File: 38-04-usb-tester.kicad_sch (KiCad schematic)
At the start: 64 parts, among them J1 Conn_1x05, J2 USB_C_12401832E402A, J3 USB_C_12401832E402A, J4 USB_Micro-B_KH-MICRO5P-JN, J5 USB_Mini-B_U-M-M5DD-W-1, J6 USB3_A_HC-USB3.0-L168-WP, SW1 SW_SPDT, SW2 ZX-1.27BM-4PSMD, U1 STM32C031K6Tx

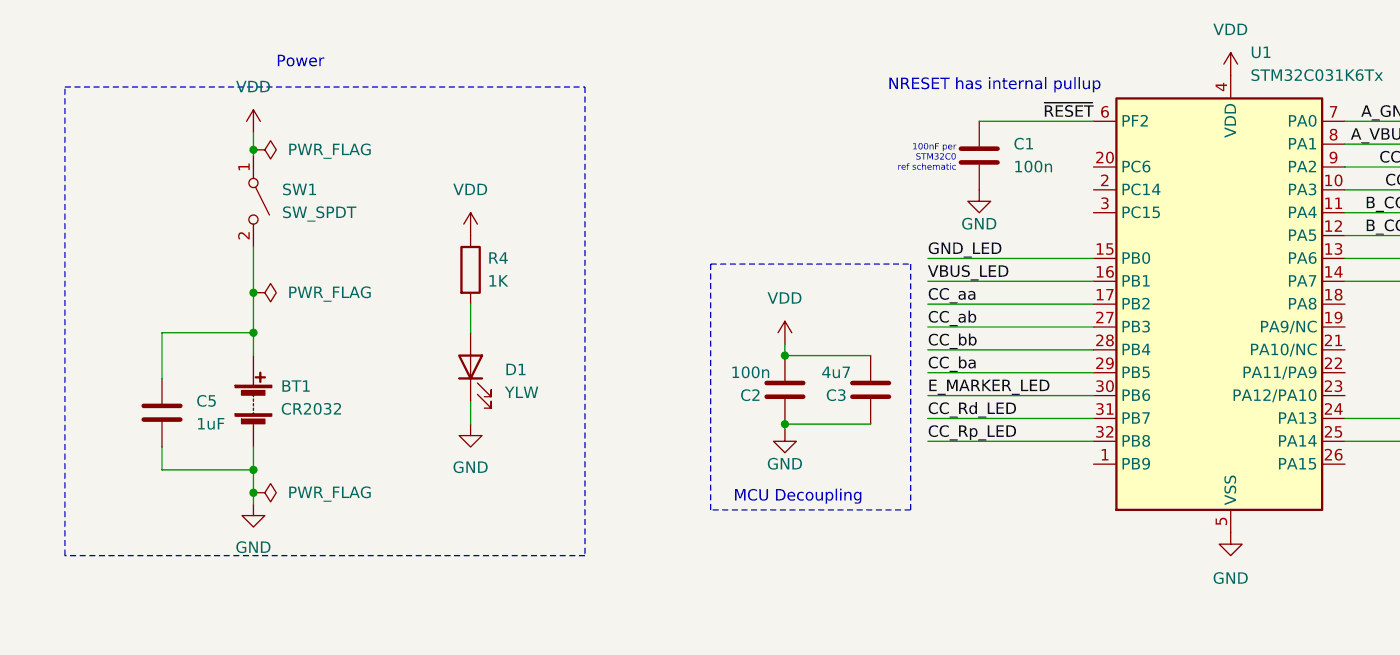
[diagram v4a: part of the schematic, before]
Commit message: more layout DRC fixes
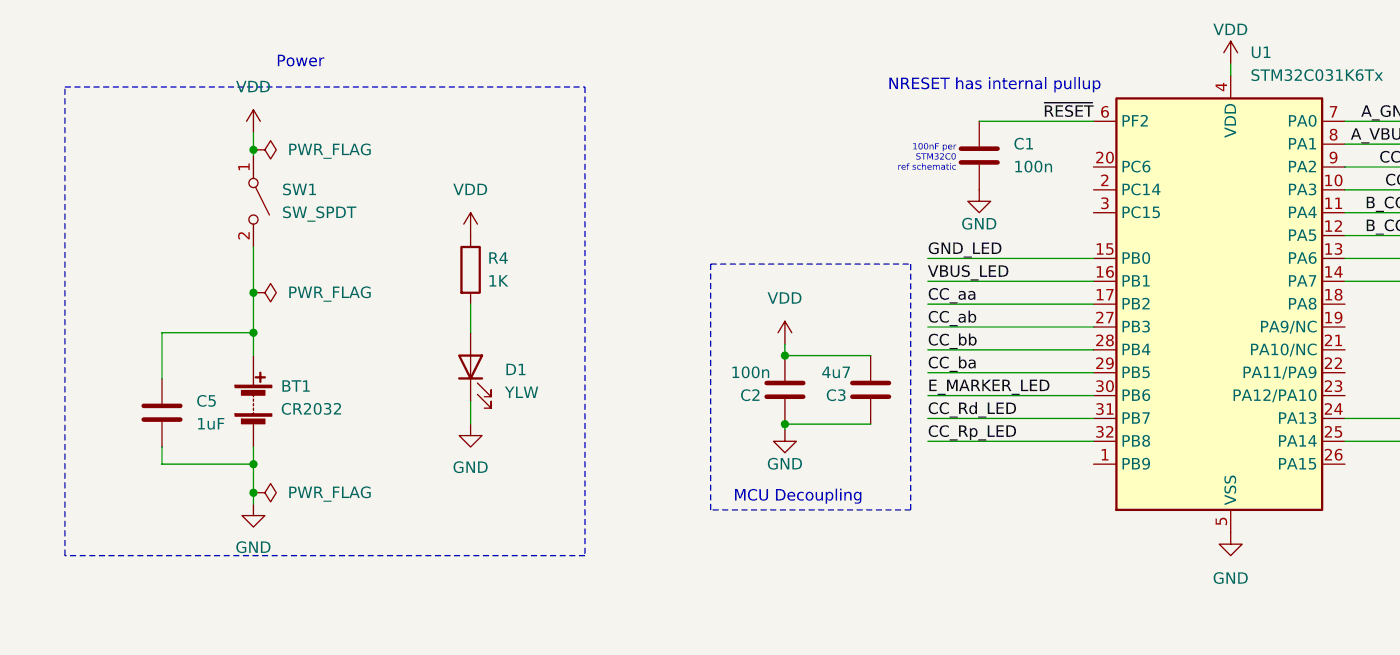
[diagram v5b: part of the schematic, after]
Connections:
- net VDD is gone; now on net VCC: U1.4 (VDD)
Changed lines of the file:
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@@
   (junction (at 218.44 139.7) (diameter 0) (color 0 0 0 0)
   )
-  (junction (at 50.165 71.12) (diameter 0) (color 0 0 0 0)
-  )
   (junction (at 182.245 106.68) (diameter 0) (color 0 0 0 0)
   )
@@
   (junction (at 45.085 163.195) (diameter 0) (color 0 0 0 0)
   )
+  (junction (at 50.165 70.485) (diameter 0) (color 0 0 0 0)
+  )
   (junction (at 367.03 161.925) (diameter 0) (color 0 0 0 0)
   )
@@
     (stroke (width 0) (type default))
   )
-  (wire (pts (xy 40.005 68.58) (xy 40.005 71.12))
-    (stroke (width 0) (type default))
-  )
   (wire (pts (xy 113.03 137.16) (xy 113.03 139.7))
     (stroke (width 0) (type default))
@@
     (stroke (width 0) (type default))
   )
-  (wire (pts (xy 40.005 71.12) (xy 50.165 71.12))
+  (wire (pts (xy 40.005 70.485) (xy 50.165 70.485))
     (stroke (width 0) (type default))
   )
@@
     (stroke (width 0) (type default))
   )
+  (wire (pts (xy 50.165 70.485) (xy 50.165 73.66))
+    (stroke (width 0) (type default))
+  )
   (wire (pts (xy 171.45 42.545) (xy 204.47 42.545))
     (stroke (width 0) (type default))
@@
     (stroke (width 0) (type default))
   )
-  (wire (pts (xy 50.165 68.58) (xy 50.165 71.12))
-    (stroke (width 0) (type default))
-  )
   (wire (pts (xy 183.515 154.94) (xy 203.835 154.94))
     (stroke (width 0) (type default))
@@
     (stroke (width 0) (type default))
   )
+  (wire (pts (xy 40.005 70.485) (xy 40.005 68.58))
+    (stroke (width 0) (type default))
+  )
   (wire (pts (xy 109.22 58.42) (xy 118.745 58.42))
     (stroke (width 0) (type default))
@@
     (stroke (width 0) (type default))
   )
+  (wire (pts (xy 158.75 26.035) (xy 158.75 27.305))
+    (stroke (width 0) (type default))
+  )
   (wire (pts (xy 182.245 106.68) (xy 194.31 106.68))
     (stroke (width 0) (type default))
@@
     (stroke (width 0) (type default))
   )
+  (wire (pts (xy 50.165 70.485) (xy 50.165 68.58))
+    (stroke (width 0) (type default))
+  )
   (wire (pts (xy 328.93 151.765) (xy 334.01 151.765))
     (stroke (width 0) (type default))
@@
     (stroke (width 0) (type default))
   )
-  (wire (pts (xy 50.165 71.12) (xy 50.165 73.66))
-    (stroke (width 0) (type default))
-  )
   (wire (pts (xy 125.095 50.165) (xy 143.51 50.165))
     (stroke (width 0) (type default))
@@
       (effects (font (size 1.27 1.27)) hide)
     )
+    (property "JLPCB_URL" "" (at 50.165 33.655 0)
+      (effects (font (size 1.27 1.27)) hide)
+    )
     (pin "1")
     (instances
@@
     )
   )
+  (symbol (lib_id "power:VCC") (at 158.75 26.035 0) (unit 1)
+    (in_bom yes) (on_board yes) (dnp no)
+    (property "Reference" "#PWR01" (at 158.75 29.845 0)
+      (effects (font (size 1.27 1.27)) hide)
+    )
+    (property "Value" "VDD" (at 158.75 22.225 0)
+      (effects (font (size 1.27 1.27)))
+    )
+    (property "Footprint" "" (at 158.75 26.035 0)
+      (effects (font (size 1.27 1.27)) hide)
+    )
+    (property "Datasheet" "" (at 158.75 26.035 0)
+      (effects (font (size 1.27 1.27)) hide)
+    )
+    (property "JLPCB_URL" "" (at 158.75 26.035 0)
+      (effects (font (size 1.27 1.27)) hide)
+    )
+    (pin "1")
+    (instances
+      (project "38-04-usb-tester"
+        (path "/450ad4bb-cada-4792-8f0e-c28850095e87"
+          (reference "#PWR01") (unit 1)
+        )
+      )
+    )
+  )
   (symbol (lib_id "Device:LED") (at 274.32 144.145 180) (unit 1)
     (in_bom yes) (on_board yes) (dnp no)
@@
         )
       )
-    )
-  )
-  (symbol (lib_name "VCC_1") (lib_id "power:VCC") (at 158.75 27.305 0) (unit 1)
-    (in_bom yes) (on_board yes) (dnp no)
-    (property "Reference" "#PWR01" (at 158.75 31.115 0)
-      (effects (font (size 1.27 1.27)) hide)
-    )
-    (property "Value" "VDD" (at 158.75 22.225 0)
-      (effects (font (size 1.27 1.27)))
-    )
-    (property "Footprint" "" (at 158.75 27.305 0)
-      (effects (font (size 1.27 1.27)) hide)
-    )
-    (property "Datasheet" "" (at 158.75 27.305 0)
-      (effects (font (size 1.27 1.27)) hide)
-    )
-    (property "JLPCB_URL" "" (at 158.75 27.305 0)
-      (effects (font (size 1.27 1.27)) hide)
-    )
-    (pin "1")
-    (instances
-      (project "38-04-usb-tester"
-        (path "/450ad4bb-cada-4792-8f0e-c28850095e87"
-          (reference "#PWR01") (unit 1)
-        )
-      )

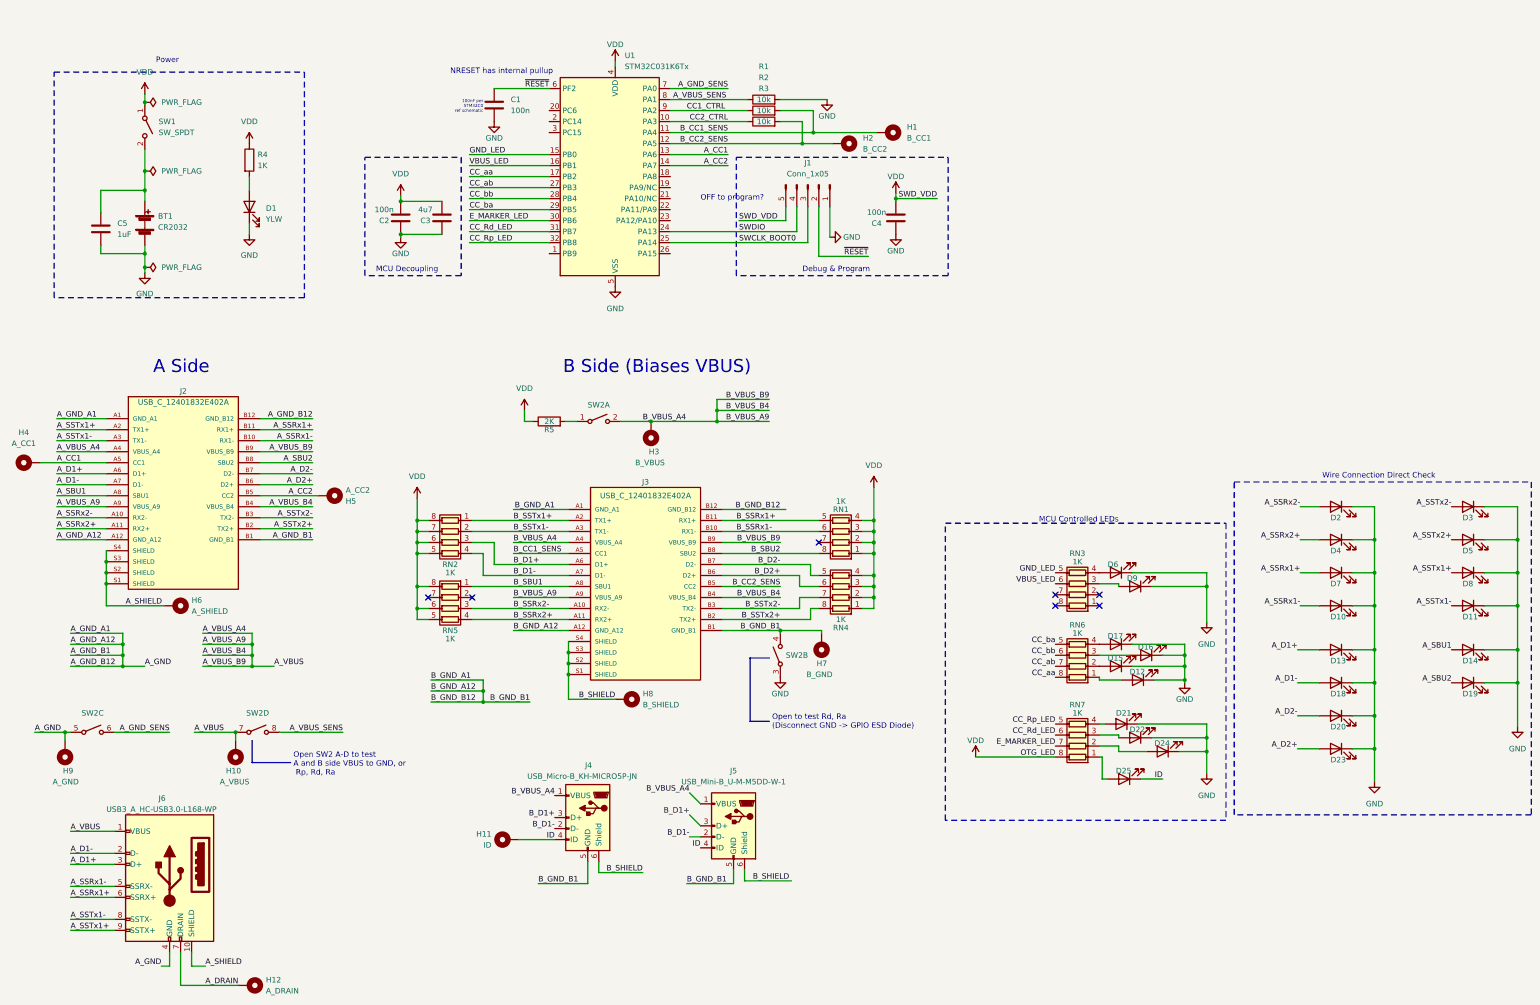
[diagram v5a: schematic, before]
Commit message: moved usb footprints from  board edge
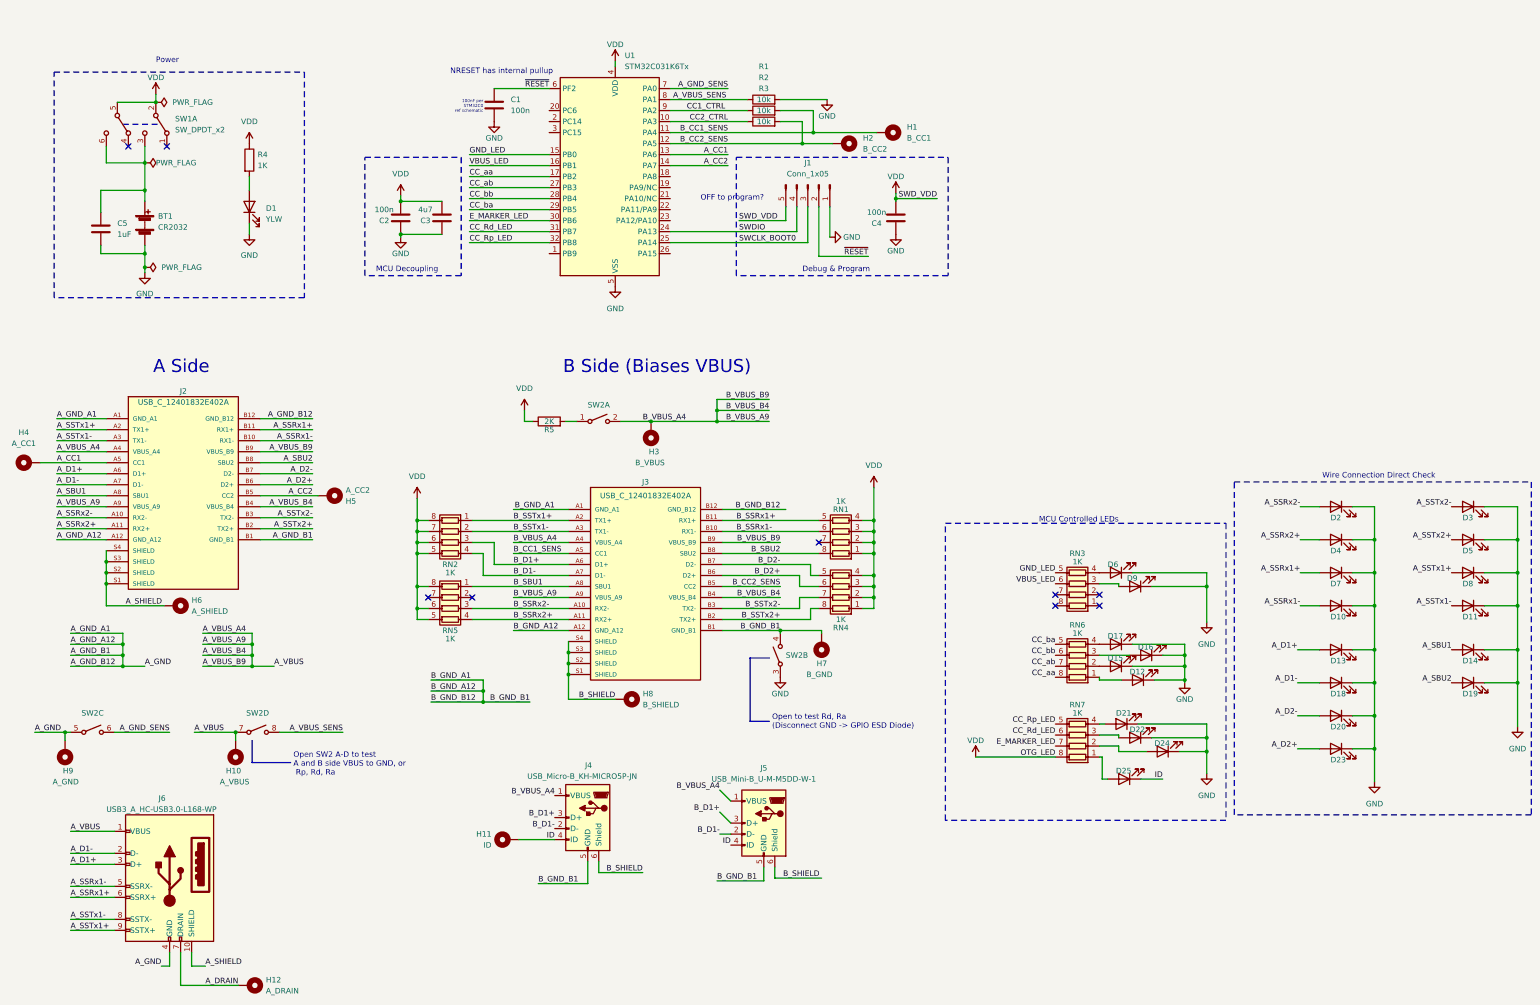
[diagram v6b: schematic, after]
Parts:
- removed SW1: SW_SPDT, Button_Switch_SMD:SW_DIP_SPSTx01_Slide_6.7x4.1mm_W8.61mm_P2.54mm_LowProfile, symbol Switch:SW_SPST
- added SW1: SW_DPDT_x2, Button_Switch_THT:SW_E-Switch_EG1271_SPDT, symbol Switch:SW_DPDT_x2
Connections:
- net VCC: now also SW1.2 (B), SW1.5 (B)
- net at BT1.1 (+), C5.1: now also SW1.3 (C), SW1.6 (C)
- no-connect marks 7 -> 9
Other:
- moved on the sheet: J5
